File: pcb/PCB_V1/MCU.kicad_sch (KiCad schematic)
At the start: 19 parts, among them J201 UART / 3V3 logic, SW201 RESET, SW202 BOOT, U201 ESP32-WROOM-32E-N4

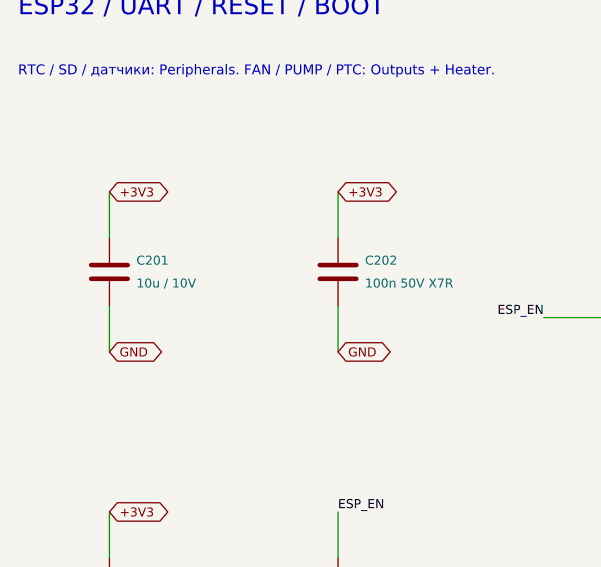
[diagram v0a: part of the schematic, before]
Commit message: pcb: revision 0.19 cost-down in the schematic, same footprints
Schematic and calculations only; PCB_V1.kicad_pcb is untouched on the
user's request. All substitutions keep footprints and nets.

- C716-C719, C726-C728: TDK C3225X7R2A106K250AC (X7R, published DC-bias
  curve 2.35 uF at 49 V) instead of Samsung CL32Y106KCV6PNE.
- C104/C105/C401: Samsung CL21A226MPQNNNE X5R; C521/C710/C715/C725/
  C905/C906: Taiyo Yuden UMK325AB7106KMHP.
- C602 shares CL21A106KAYNNNE with C201 (1.41 uF screen >= 1 uF);
  D601 shares SMBJ26CA with D901 (D_TVS symbol, 42.1 V clamp);
  R501/R511/R521 33R; F904 3 A shared with F721.
- analyze_led_power/analyze_power_path/verify_netlist updated; price and
  JLC snapshots v19; reports, sheet images and checks log v19.
- COST_DOWN.md: USD 37.50 per board (was 39.82), 65 purchase codes,
  rejected candidates and board status.

verify_board.py reports value differences for 17 parts until the board
is synced (footprints and nets already match); all other checks pass.

Co-Authored-By: Claude Opus 5.5 <noreply@anthropic.com>
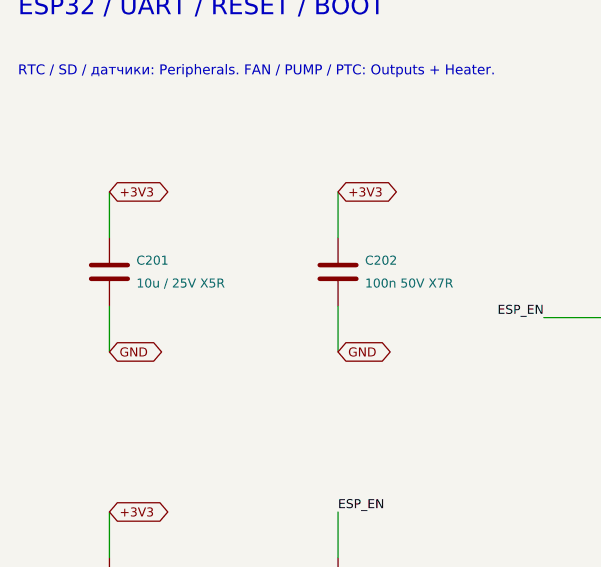
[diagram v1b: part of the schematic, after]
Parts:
- C201: value 10u / 10V -> 10u / 25V X5R; LCSC (none) -> C15850; MPN (none) -> CL21A106KAYNNNE; Manufacturer (none) -> Samsung Electro-Mechanics
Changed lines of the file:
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@@
 			)
 		)
-		(property "Value" "10u / 10V"
+		(property "Value" "10u / 25V X5R"
 			(at 33.48 46.99 0)
 			(show_name no)
@@
 			)
 		)
-		(property "Datasheet" ""
+		(property "Datasheet" "https://product.samsungsem.com/mlcc/CL21A106KAYNNN.do"
 			(at 30.48 45.72 0)
 			(hide yes)
@@
 			)
 		)
+		(property "Manufacturer" "Samsung Electro-Mechanics"
+			(at 30.48 45.72 0)
+			(effects
+				(font
+					(size 1 1)
+				)
+				(hide yes)
+			)
+		)
+		(property "LCSC" "C15850"
+			(at 30.48 45.72 0)
+			(effects
+				(font
+					(size 1 1)
+				)
+				(hide yes)
+			)
+		)
+		(property "MPN" "CL21A106KAYNNNE"
+			(at 30.48 45.72 0)
+			(effects
+				(font
+					(size 1 1)
+				)
+				(hide yes)
+			)
+		)
